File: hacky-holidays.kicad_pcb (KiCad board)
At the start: 2 copper layers, 96 x 99.7 mm, 45 parts, among them J1 Conn_01x04_Pin, Q1 AO3401A, Q2 AO3400A, Q3 AO3400A, SW1 SW_Push, SW2 SW_Push, SW3 SW_Push, SW4 SW_SPDT, U1 TP4057, U2 CH552G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

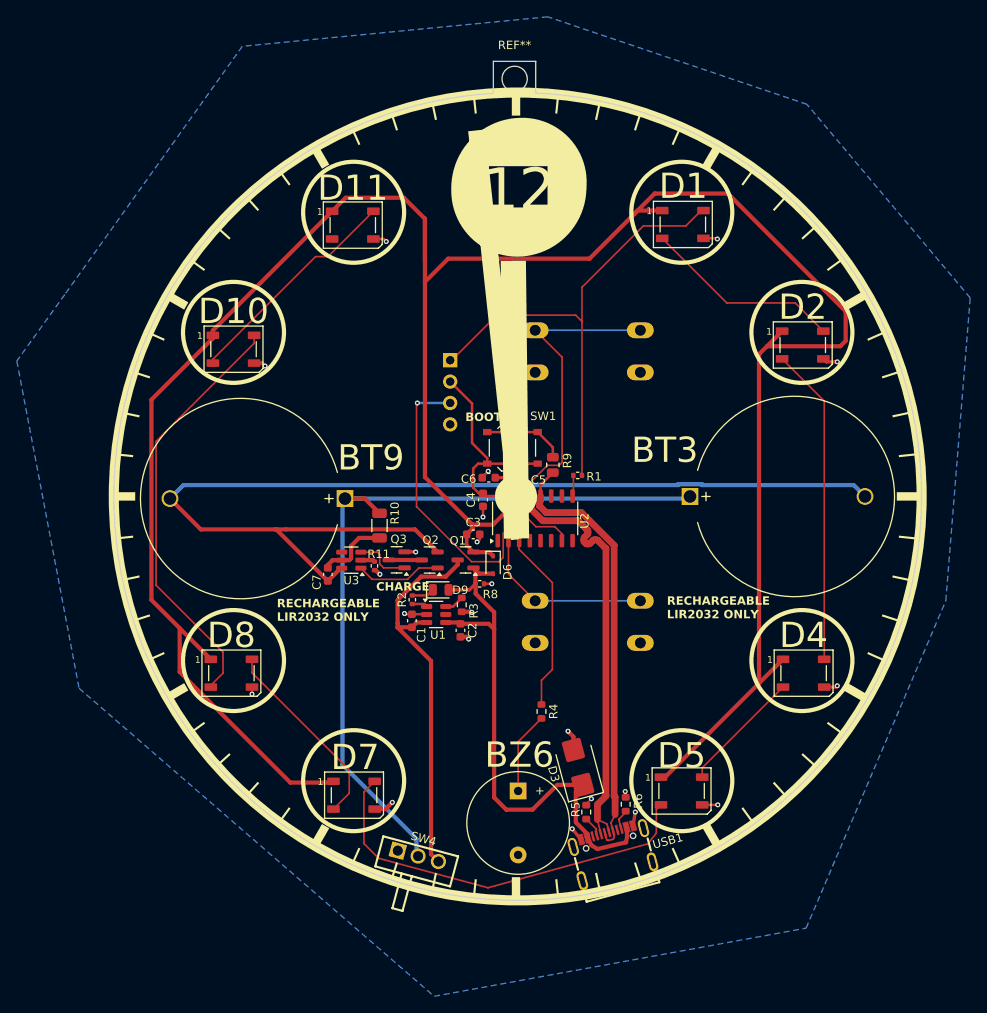
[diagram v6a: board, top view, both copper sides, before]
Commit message: use economic ws2812bs
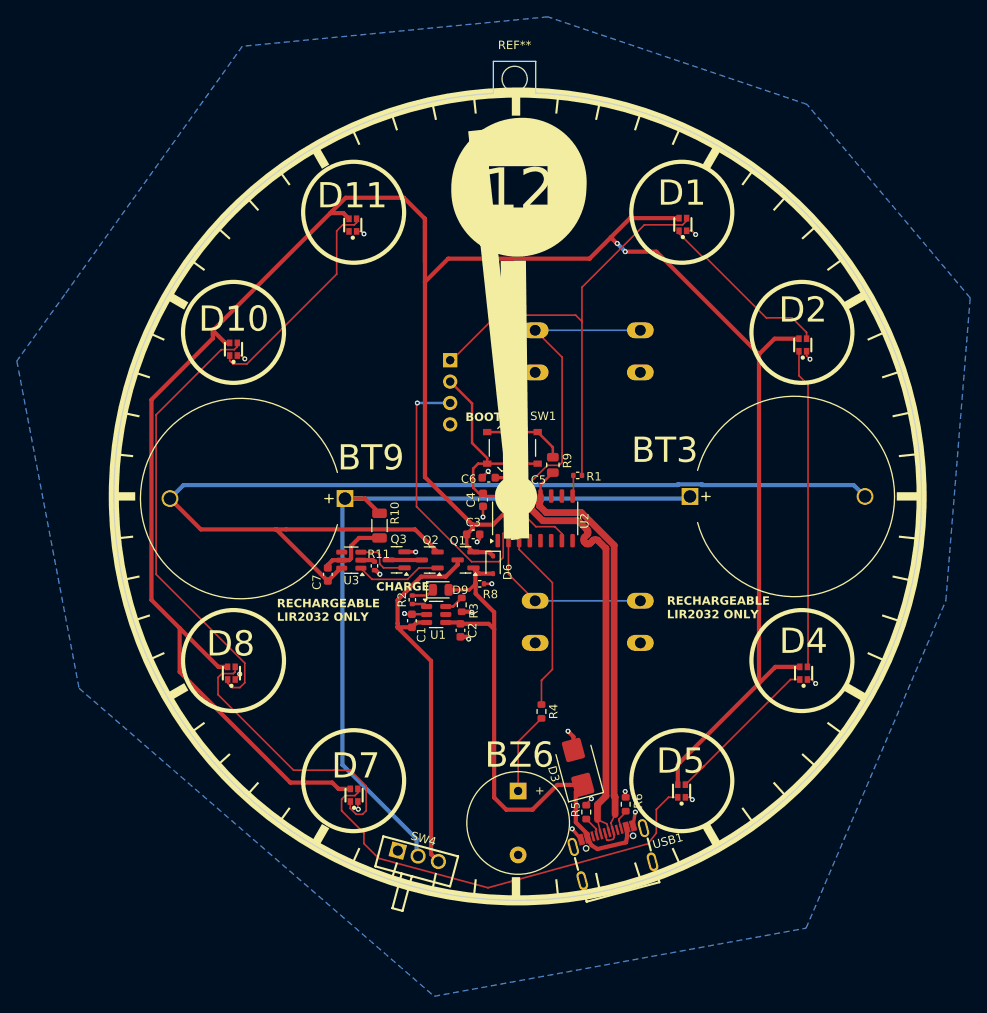
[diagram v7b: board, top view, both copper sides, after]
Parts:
- D1, D10, D11, D2, D4, D5, D7, D8: footprint LED_SMD:LED_WS2812B_PLCC4_5.0x5.0mm_P3.2mm -> lcsc-imports:LED-SMD_4P-L1.6-W1.5_XL-1615RGBC-WS2812B
- turned D1 to 90 degrees
- turned D10 to 90 degrees
- turned D11 to 90 degrees
- turned D2 to 90 degrees
- turned D4 to 90 degrees
- turned D5 to 90 degrees
- turned D7 to 90 degrees
- turned D8 to 90 degrees
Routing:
- net Net-(D7-DOUT): track 23.4 -> 33.1 mm
- net +5V: track 307.9 -> 300.6 mm, vias 0 -> 2
- net GND: track 35.0 -> 30.0 mm
- net Net-(D4-DOUT): track 14.7 -> 19.1 mm
- net Net-(D5-DOUT): track 48.8 -> 52.3 mm
- net Net-(D1-DOUT): track 23.7 -> 21.1 mm
- net WS2812B: track 58.7 -> 56.5 mm
- net Net-(D10-DIN): track 50.5 -> 52.6 mm
- net Net-(D10-DOUT): track 26.8 -> 26.3 mm

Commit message: fix designators
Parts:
- D10: value WS2812B -> D10
- D11: value WS2812B -> D11
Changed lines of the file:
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@@
 		(layer "F.Cu")
 		(at 187.425 42.25 90)
-		(property "Value" "WS2812B"
+		(property "Value" "D11"
 			(at 0 4.45 90)
 			(layer "F.Fab")
@@
 			)
 		)
-		(property "Footprint" ""
+		(property "Footprint" "WS2812B"
 			(at 0 0 90)
 			(layer "F.Fab")
@@
 		(layer "F.Cu")
 		(at 173.25 57 90)
-		(property "Value" "WS2812B"
+		(property "Value" "D10"
 			(at 0 4.45 90)
 			(layer "F.Fab")
@@
 			)
 		)
-		(property "Footprint" ""
+		(property "Footprint" "WS2812B"
 			(at 0 0 90)
 			(layer "F.Fab")
